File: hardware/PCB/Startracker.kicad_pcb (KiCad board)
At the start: 4 copper layers, 99.8 x 99.8 mm, 135 parts, among them IC1 BNO085, IC2 IIS2MDCTR, J1 IMU_EXT, J2 GPS, J3 Motor1, J4 Motor2, J5 Motor3, J6 6V, J7 SJ-3523-SMT-TR, J8 USB_C_Receptacle_USB2.0_16P, Q1 2N3904, Q2 2N3904, SW1 RST, SW2 BOOT, SW3 PWR, U1 ESP32-S3-WROOM-1, U10 SX1261IMLTRT, U11 BGS12P2L6E6327XT, U12 SRV05-4, U13 TPS54308, U14 TPS2121RUXR, U2 TMC2209-LA, U3 TB6612FNG, U4 TB6612FNG, U5 PCF8574T, U7 BME280, U8 INA219BxDCN, U9 INA219BxDCN, Y1 Crystal, Y2 32.00 MHz

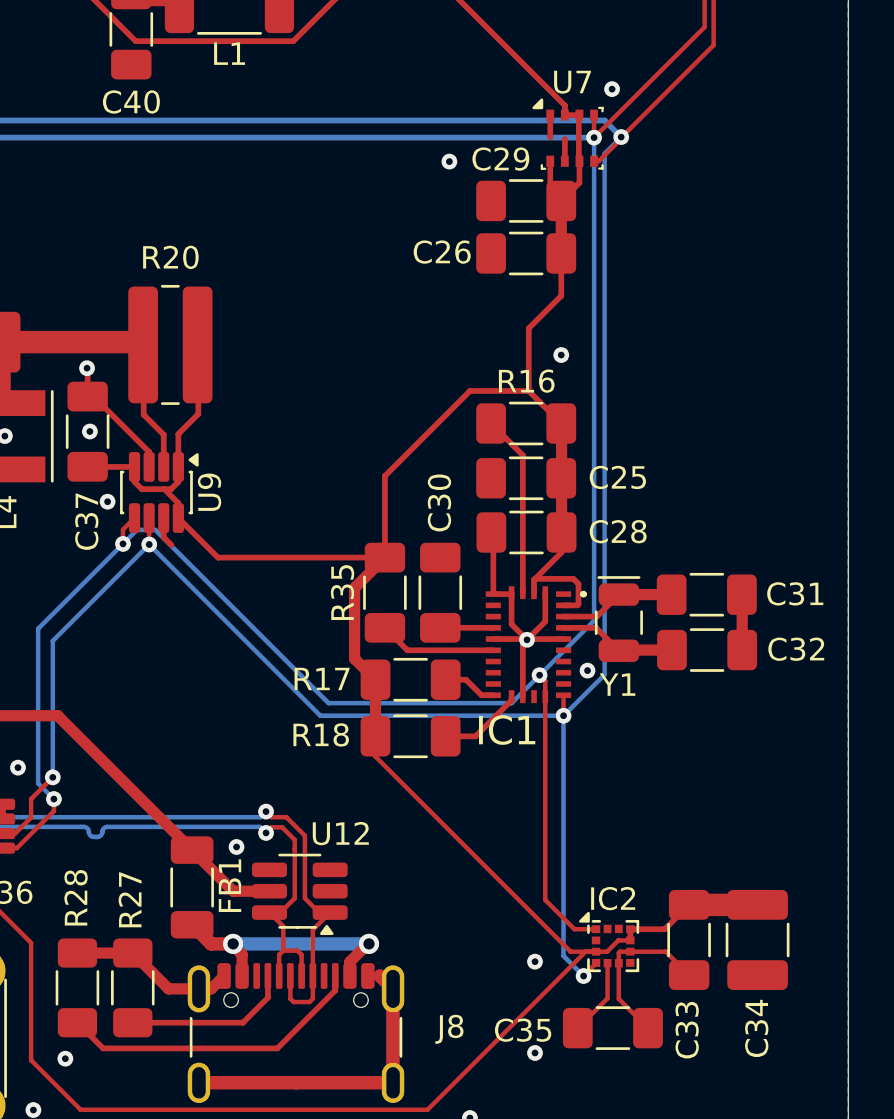
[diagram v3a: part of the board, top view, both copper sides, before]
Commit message: Routed VL53L4CD
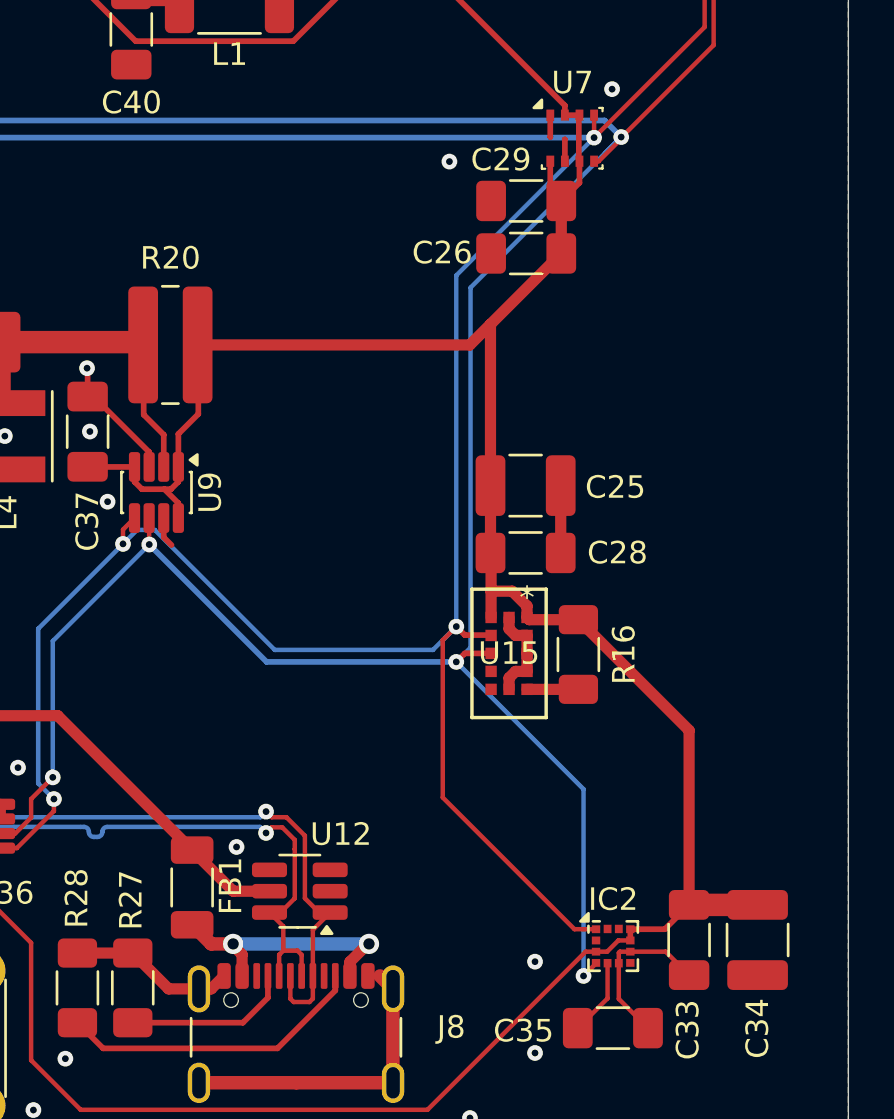
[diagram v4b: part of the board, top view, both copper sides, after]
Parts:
- removed C30: 100n, Capacitor_SMD:C_1206_3216Metric_Pad1.33x1.80mm_HandSolder
- removed C31, C32: 22p, Capacitor_SMD:C_1206_3216Metric_Pad1.33x1.80mm_HandSolder
- removed IC1: BNO085, BNO085:BNO085
- removed R17, R18: 4k7, Capacitor_SMD:C_1206_3216Metric_Pad1.33x1.80mm_HandSolder
- removed R35: 10k, Capacitor_SMD:C_1206_3216Metric_Pad1.33x1.80mm_HandSolder
- removed Y1: Crystal, Crystal:Crystal_SMD_MicroCrystal_CC7V-T1A-2Pin_3.2x1.5mm
- added U15: VL53L4CDV0DH/1, footprints:LGA12_STM, F.Cu at (175.9, 127.2)
- C25: value 100n -> 10u; footprint Capacitor_SMD:C_1206_3216Metric_Pad1.33x1.80mm_HandSolder -> Capacitor_SMD:C_1210_3225Metric_Pad1.33x2.70mm_HandSolder
- R16: footprint Capacitor_SMD:C_1206_3216Metric_Pad1.33x1.80mm_HandSolder -> Resistor_SMD:R_1206_3216Metric_Pad1.30x1.75mm_HandSolder
- moved R16 10.5 mm to (179.0, 127.3), turned to 90 degrees
- moved C28 0.91 mm to (176.6, 122.7), turned to 180 degrees
- moved C25 0.33 mm to (176.6, 119.7), turned to 180 degrees
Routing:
- net +3.3V: track 458.6 -> 443.8 mm
- net GND: track 187.7 -> 178.5 mm, vias 88 -> 85
- net Net-(U15-XSHUT): track 8.12 -> 2.29 mm
- net Net-(IC1-XOUT32/CLKSEL1): track 5.26 -> 0.00 mm
- net Net-(IC1-NRST): track 5.24 -> 0.00 mm
- net Net-(IC1-XIN32): track 5.22 -> 0.00 mm
- net Net-(IC1-ENV_SDA): track 3.76 -> 0.00 mm
- net Net-(IC1-ENV_SCL_): track 2.40 -> 0.00 mm
- net Net-(IC1-CAP): track 2.36 -> 0.00 mm
- net /OBC/I2C_SCL: track 187.9 -> 188.4 mm

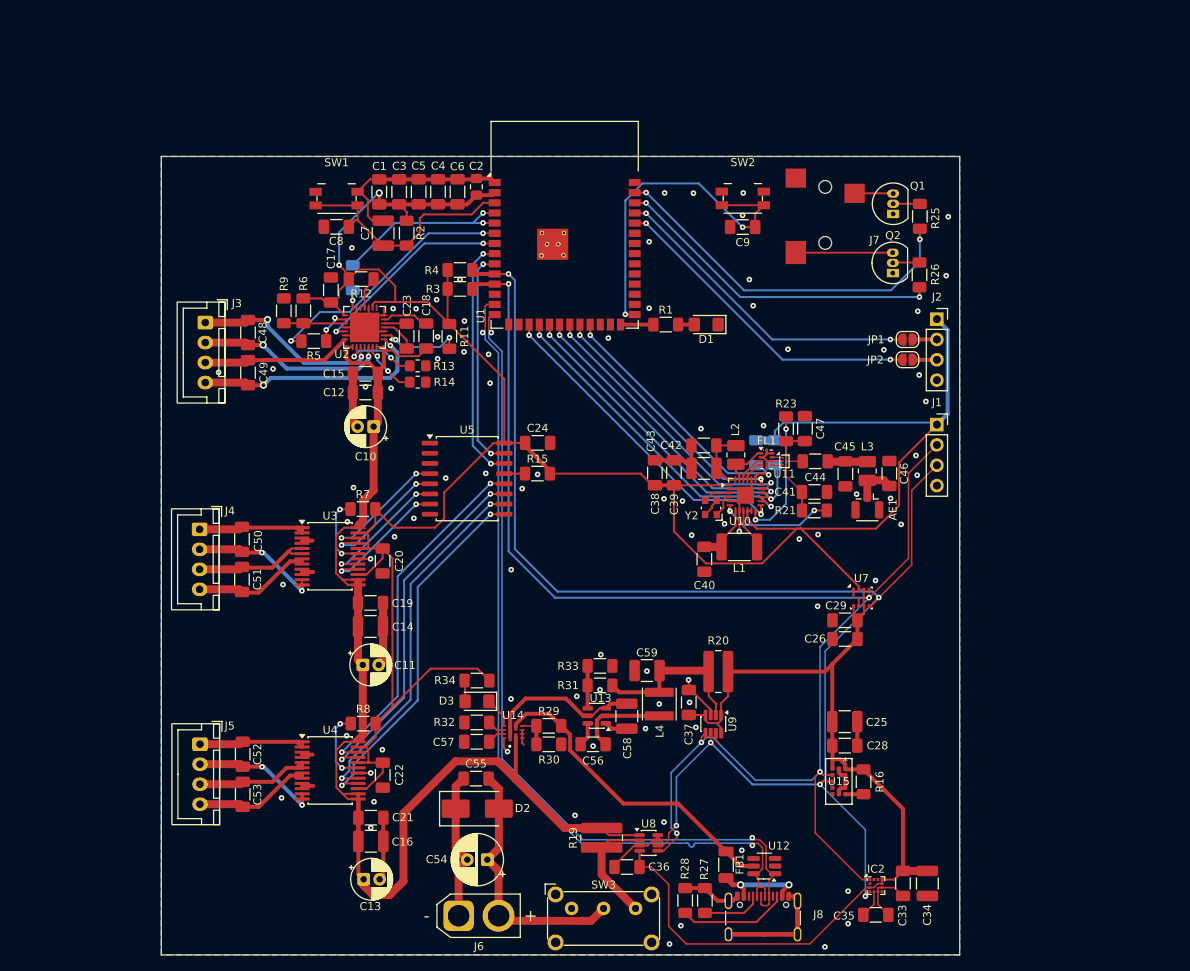
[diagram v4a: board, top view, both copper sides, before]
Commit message: added external ToF instead of on-PCB
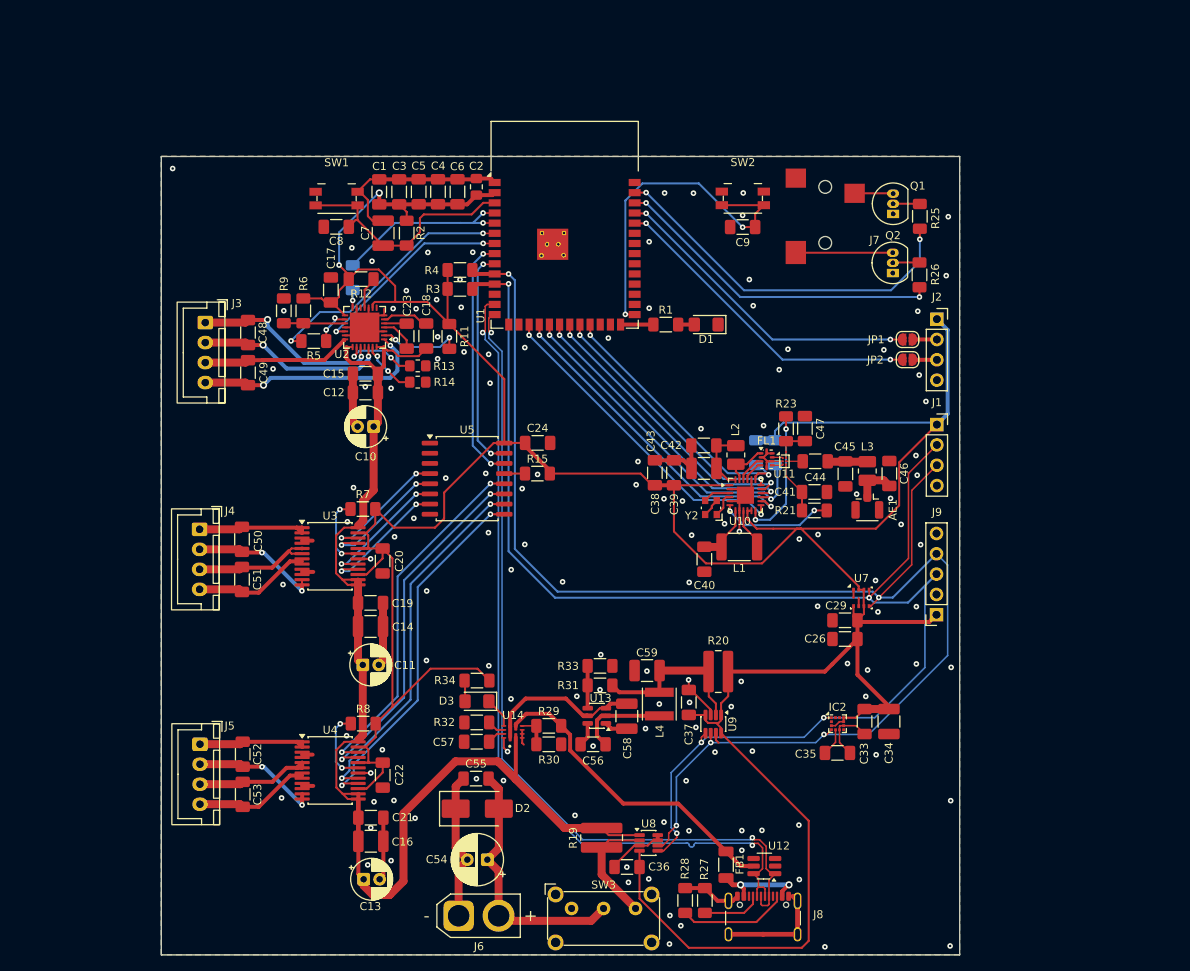
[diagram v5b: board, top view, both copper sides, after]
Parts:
- removed C25: 10u, Capacitor_SMD:C_1210_3225Metric_Pad1.33x2.70mm_HandSolder
- removed C28: 100n, Capacitor_SMD:C_1206_3216Metric_Pad1.33x1.80mm_HandSolder
- removed R16: 10k, Resistor_SMD:R_1206_3216Metric_Pad1.30x1.75mm_HandSolder
- removed U15: VL53L4CDV0DH/1, footprints:LGA12_STM
- added J9: Conn_01x05_Socket, Connector_PinSocket_2.54mm:PinSocket_1x05_P2.54mm_Vertical, F.Cu at (188.1, 106.4)
- moved C35 20.8 mm to (175.7, 123.6)
- moved C33 20.8 mm to (179.1, 119.7)
- moved C34 20.8 mm to (182.1, 119.7)
- moved IC2 20.8 mm to (175.7, 120.0)
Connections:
- U1 pad 31: unconnected-(U1-IO38-Pad31) -> /OBC/VL_GPIO1
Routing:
- net +3.3V: track 443.8 -> 451.7 mm
- net GND: track 178.5 -> 171.1 mm, vias 85 -> 130
- net /OBC/I2C_SCL: track 188.4 -> 182.7 mm
- net /OBC/I2C_SDA: track 188.0 -> 184.0 mm, vias 6 -> 5
- net Net-(U15-XSHUT): track 2.29 -> 0.00 mm

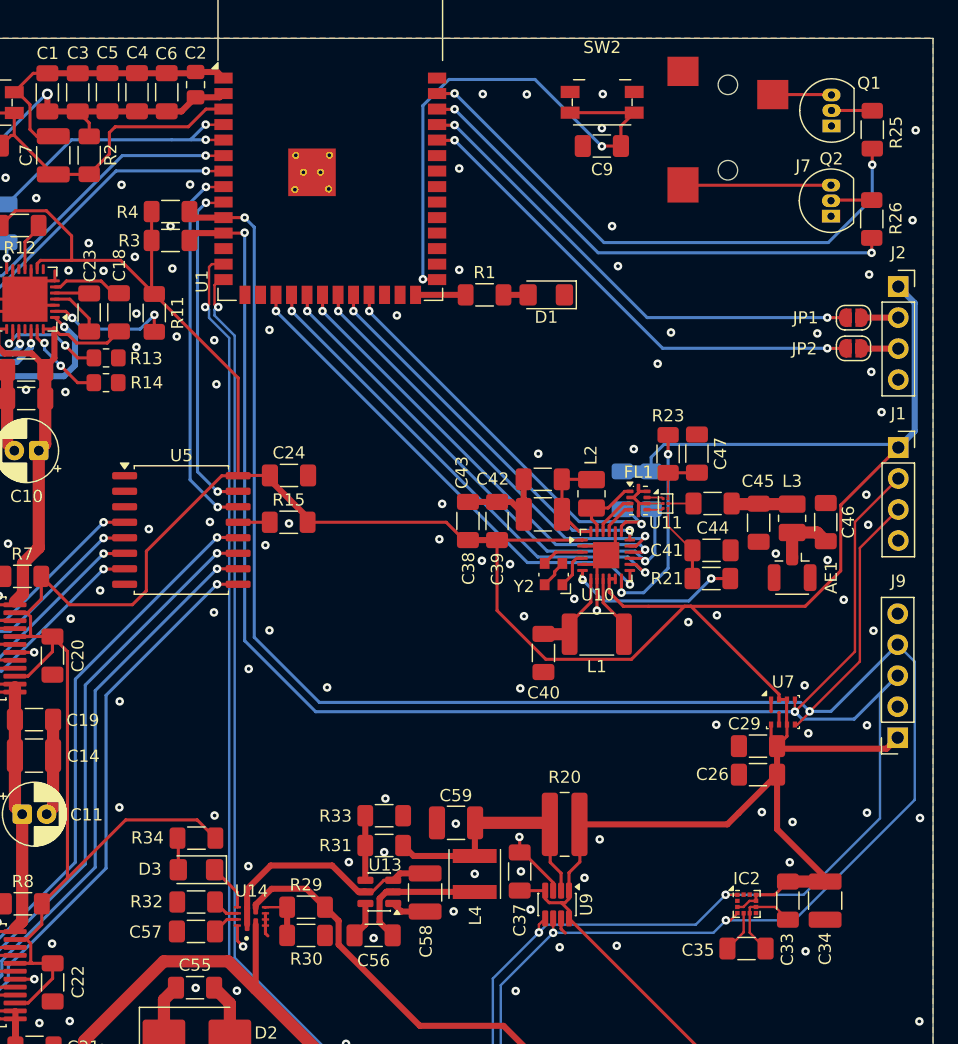
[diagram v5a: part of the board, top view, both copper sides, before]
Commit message: Added external QMC5883L instead of on-PCB IIS2MDCTR
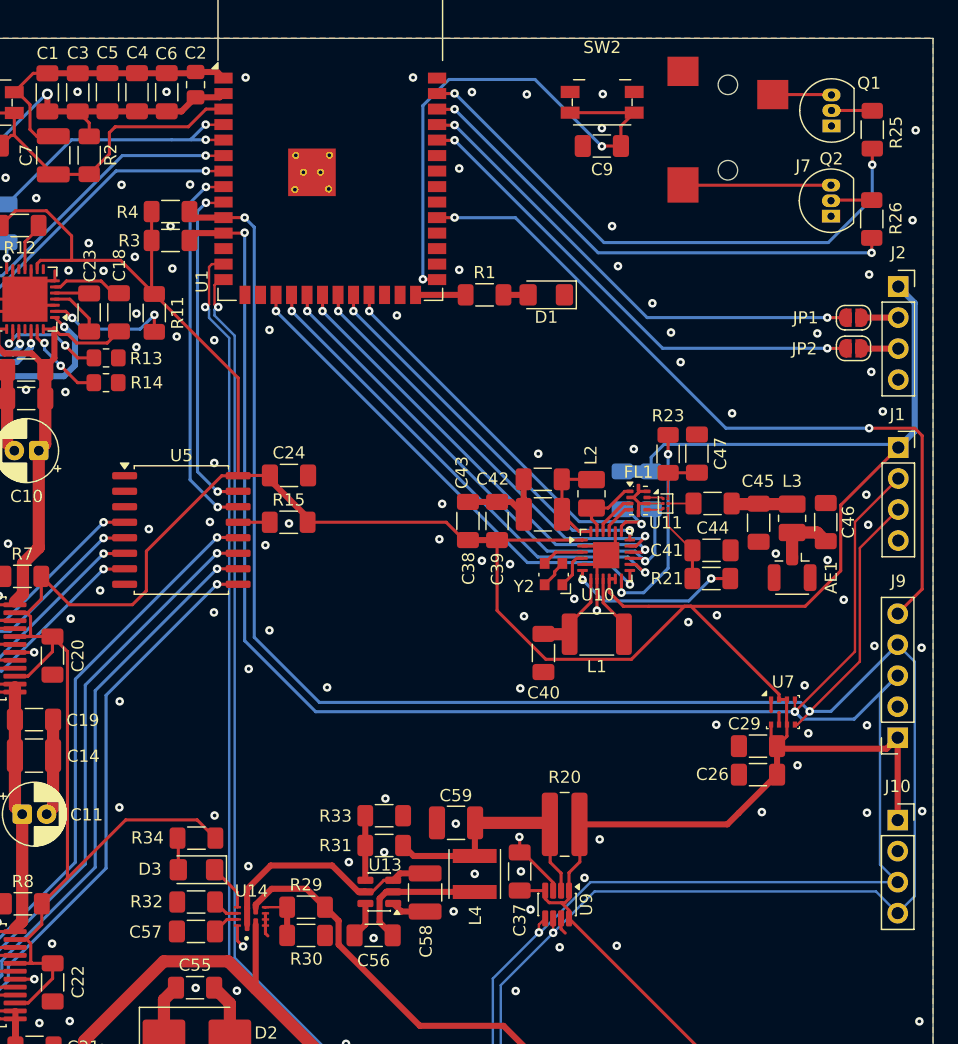
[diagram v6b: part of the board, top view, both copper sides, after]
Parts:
- removed C33: 100n, Capacitor_SMD:C_1206_3216Metric_Pad1.33x1.80mm_HandSolder
- removed C34: 10u, Capacitor_SMD:C_1210_3225Metric_Pad1.33x2.70mm_HandSolder
- removed C35: 220n, Capacitor_SMD:C_1206_3216Metric_Pad1.33x1.80mm_HandSolder
- removed IC2: IIS2MDCTR, Package_LGA:LGA-12_2x2mm_P0.5mm
- added J10: Conn_01x04_Socket, Connector_PinSocket_2.54mm:PinSocket_1x04_P2.54mm_Vertical, F.Cu at (188.1, 113.1)
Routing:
- net /OBC/VL_GPIO1: track 0.00 -> 62.5 mm, vias 0 -> 2
- net +3.3V: track 451.7 -> 439.8 mm
- net GND: track 171.1 -> 163.6 mm, vias 130 -> 135
- net /OBC/I2C_SDA: track 184.0 -> 188.9 mm, vias 5 -> 4
- net /OBC/I2C_SCL: track 182.7 -> 186.9 mm, vias 5 -> 4
- net Net-(IC2-C1): track 3.44 -> 0.00 mm
